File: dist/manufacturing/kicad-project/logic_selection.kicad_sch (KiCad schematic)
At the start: 10 parts, among them U23 LM66100DCKR, U24 LM66100DCKR, U4 SN74LVC1G08DBVR

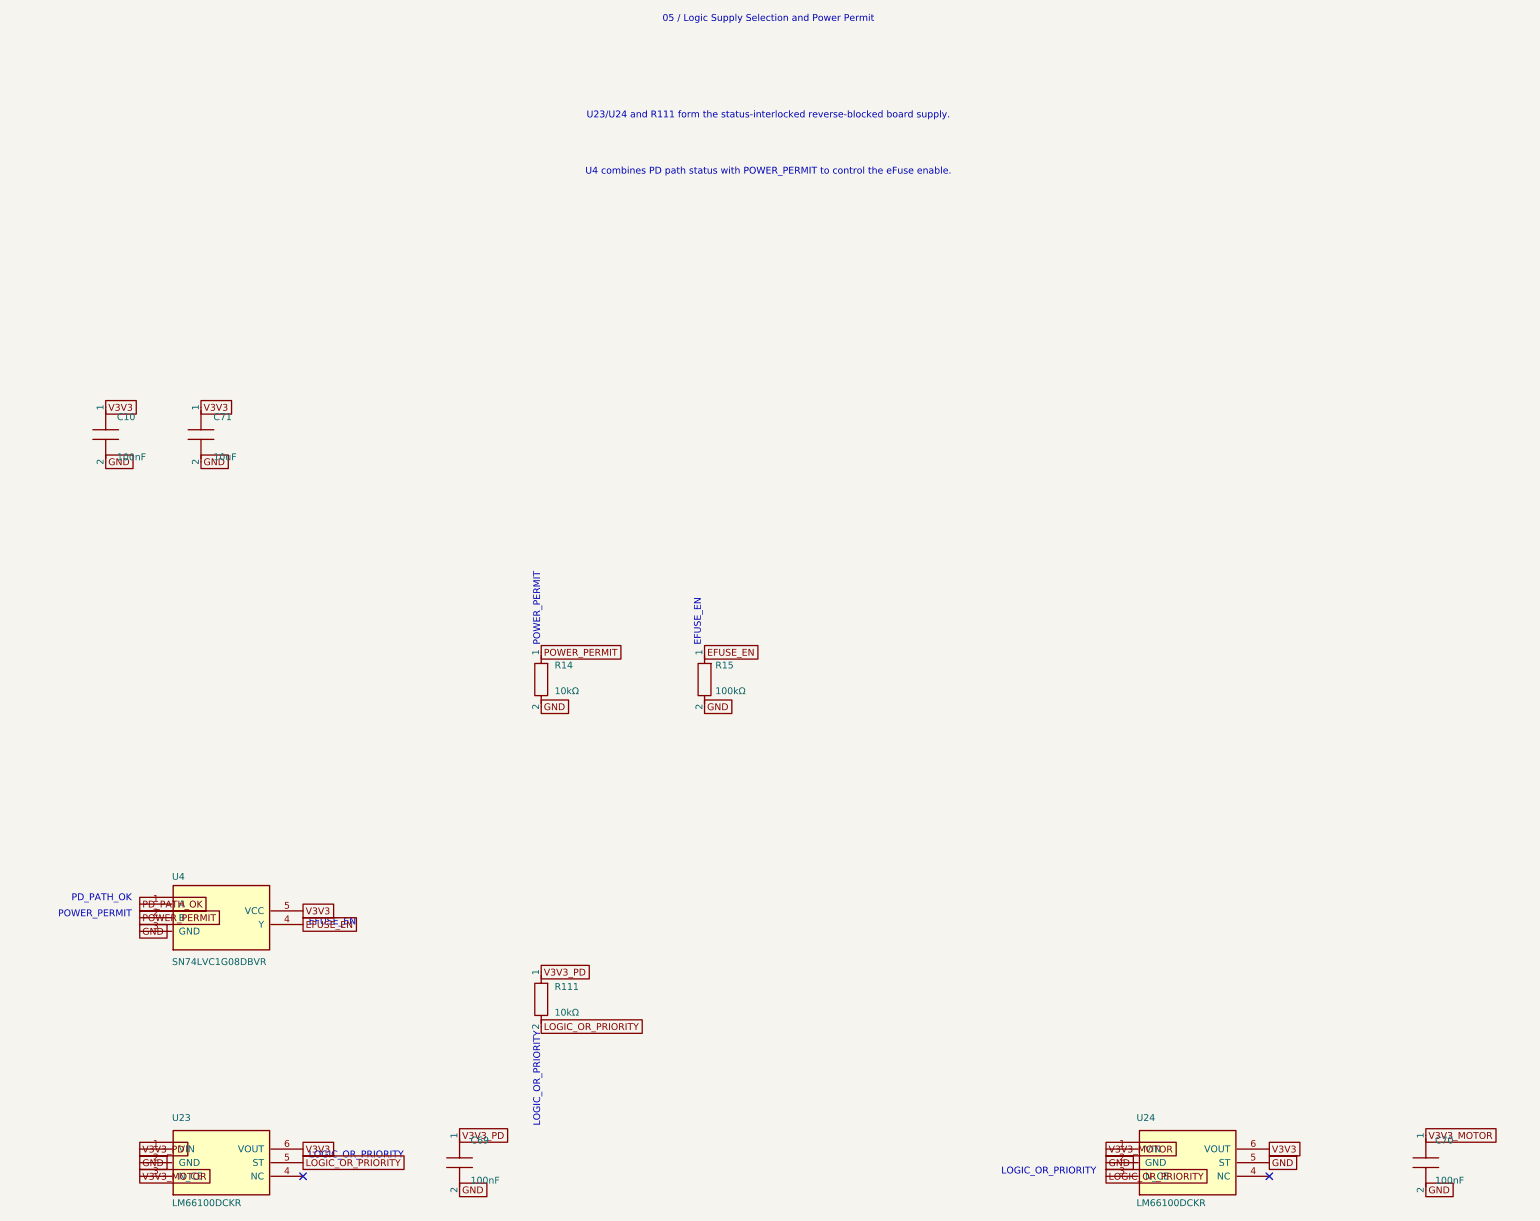
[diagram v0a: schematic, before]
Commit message: Implement motor harness and mounting; remove unsupported interfaces
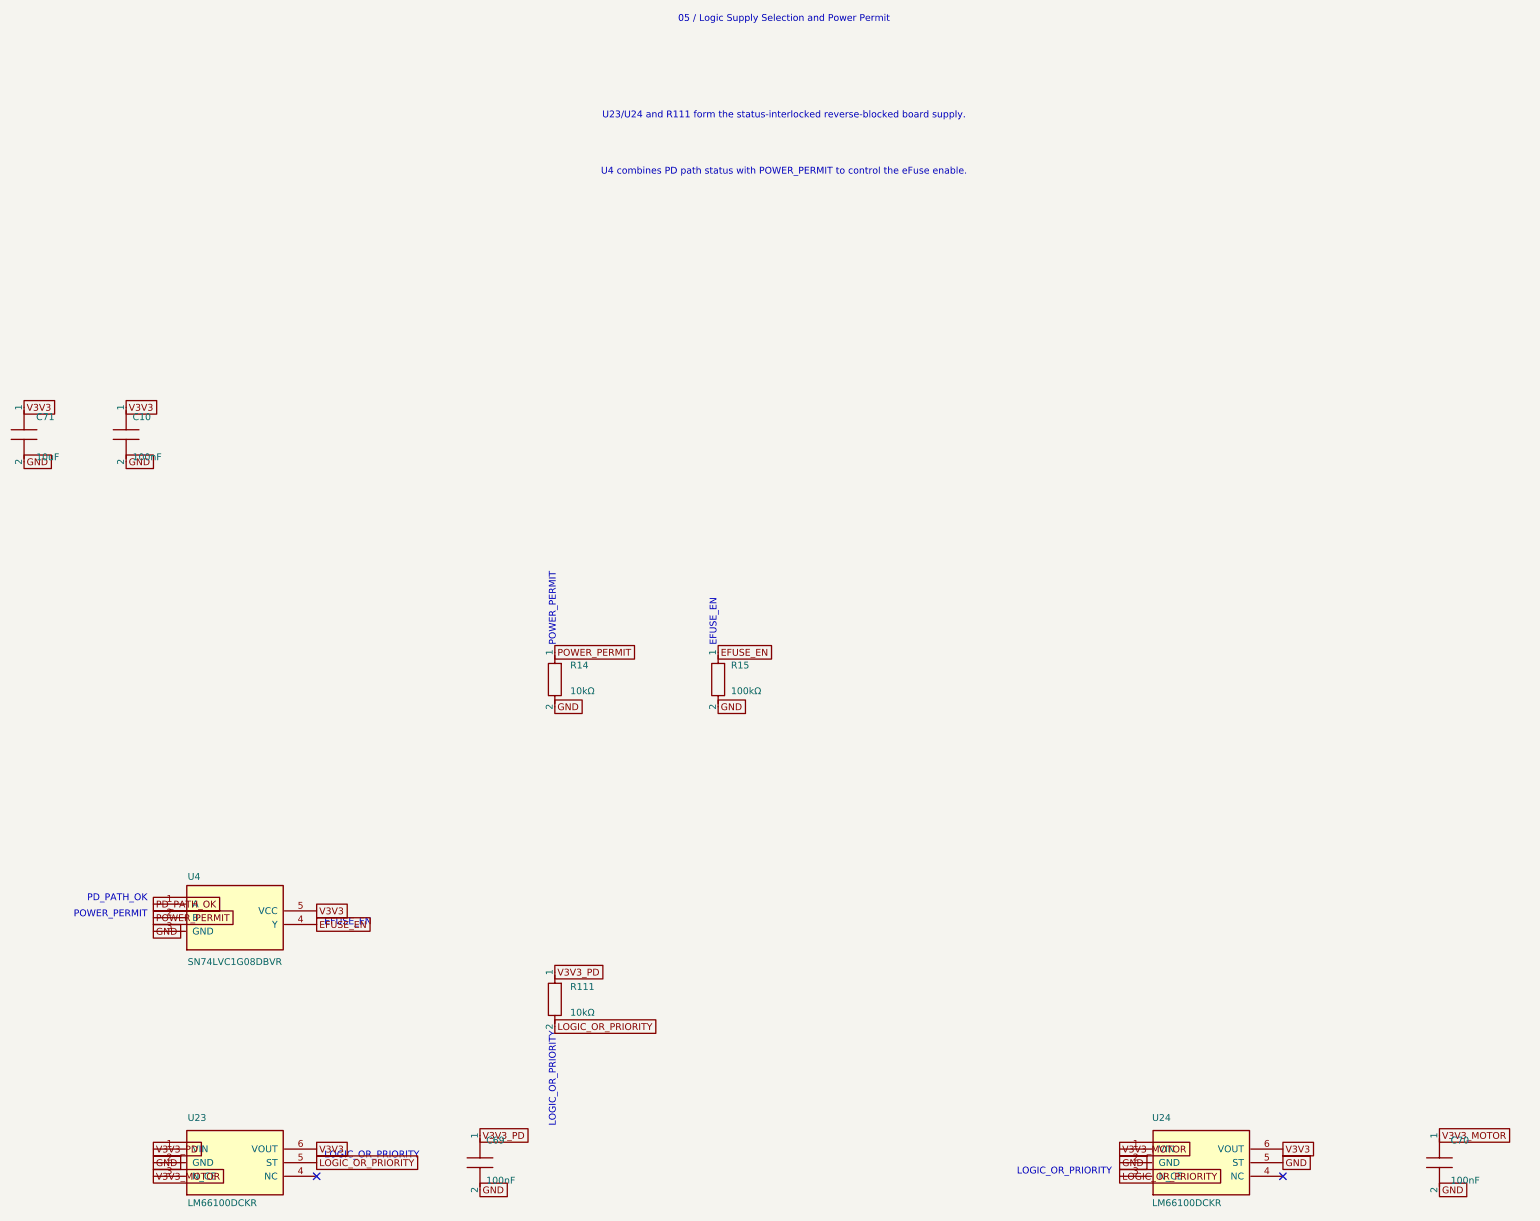
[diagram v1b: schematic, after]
